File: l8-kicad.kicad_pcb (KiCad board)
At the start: 4 copper layers, 55.5 x 89.5 mm, 122 parts, among them J1 USB_B_Mini, J2 LCD 3.2" 240x320 Conn_01x14_P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, J3 Screw_Terminal_01x06, J4 Conn_ST_STDC14, J7 TC2030 - TAG Connect, Q1 SI2301CDS-T1-GE3, Q4 SI2301CDS-T1-GE3, Q5 SI2301CDS-T1-GE3, SW1 SW_Push, SW2 SW_Push, U1 B0505S-1WR2, U2 ISO1042-Q1, U22 TLV76733DRVx, U3 STM32F427V_G-I_Tx, U4 ST_SENSOR_2, U5 IIS3DHHCTR, X1 8MHz 20pF

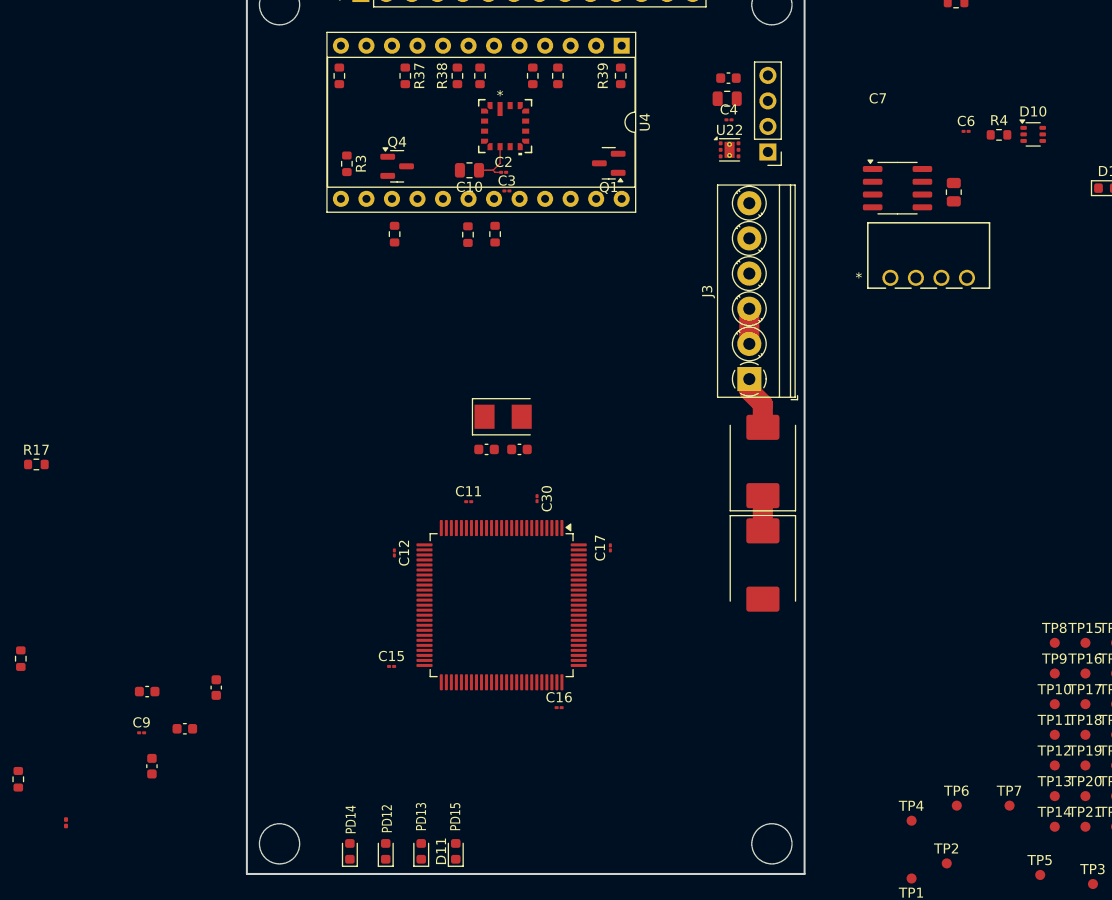
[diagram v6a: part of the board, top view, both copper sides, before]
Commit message: pre-quilter after cap size issue
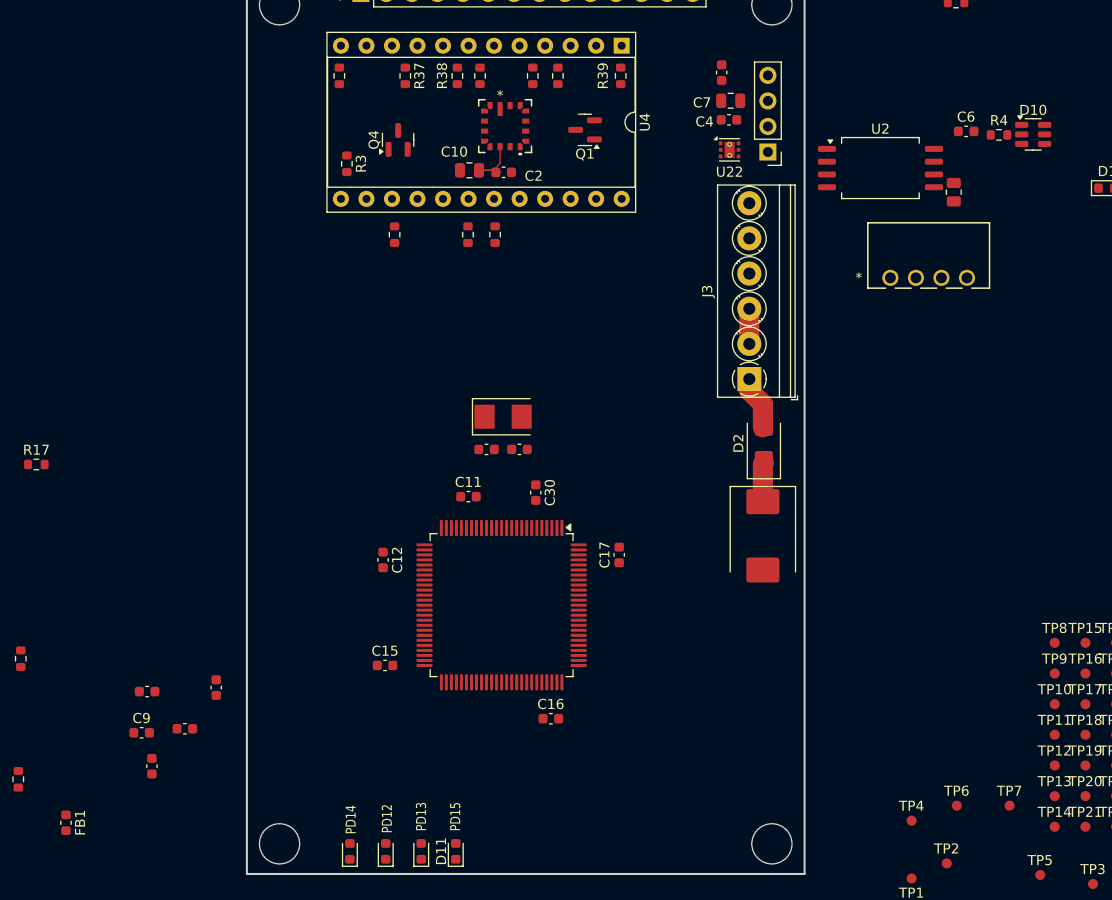
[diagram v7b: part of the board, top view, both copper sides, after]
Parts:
- removed C3: 100nF, Capacitor_SMD:C_01005_0402Metric
- C11, C12, C15, C16, C17, C2, C30, C4, C6, C9: footprint Capacitor_SMD:C_01005_0402Metric -> Capacitor_SMD:C_0603_1608Metric
- D10: footprint Package_TO_SOT_SMD:SOT-363_SC-70-6 -> Package_TO_SOT_SMD:SOT-23-6
- D2: footprint Diode_SMD:D_SMC -> Diode_SMD:D_SMA
- FB1: value FILTER -> ~; footprint Resistor_SMD:R_0201_0603Metric -> Inductor_SMD:L_0603_1608Metric
- U2: footprint Package_SO:SOIC-8_3.9x4.9mm_P1.27mm -> Package_SO:SOIC-8_7.5x5.85mm_P1.27mm
- moved Q1 4.08 mm to (133.7, 115.5)
- moved D3 2.90 mm to (151.3, 155.8)
- moved Q4 2.63 mm to (115.0, 116.5), turned to 90 degrees
- moved U2 2.62 mm to (163.1, 119.2)
- moved D2 1.80 mm to (151.4, 146.7)
- moved C16 1.38 mm to (130.2, 174.1)
- moved C12 1.32 mm to (113.5, 158.2)
- moved C17 1.12 mm to (137.1, 157.8)
- moved C5 0.87 mm to (147.2, 109.8), turned to -90 degrees
- moved C15 0.66 mm to (113.8, 168.8)
- moved C30 0.61 mm to (128.8, 151.6)
- moved C11 0.50 mm to (122.0, 151.9)
- moved C7 0.40 mm to (148.2, 112.5)

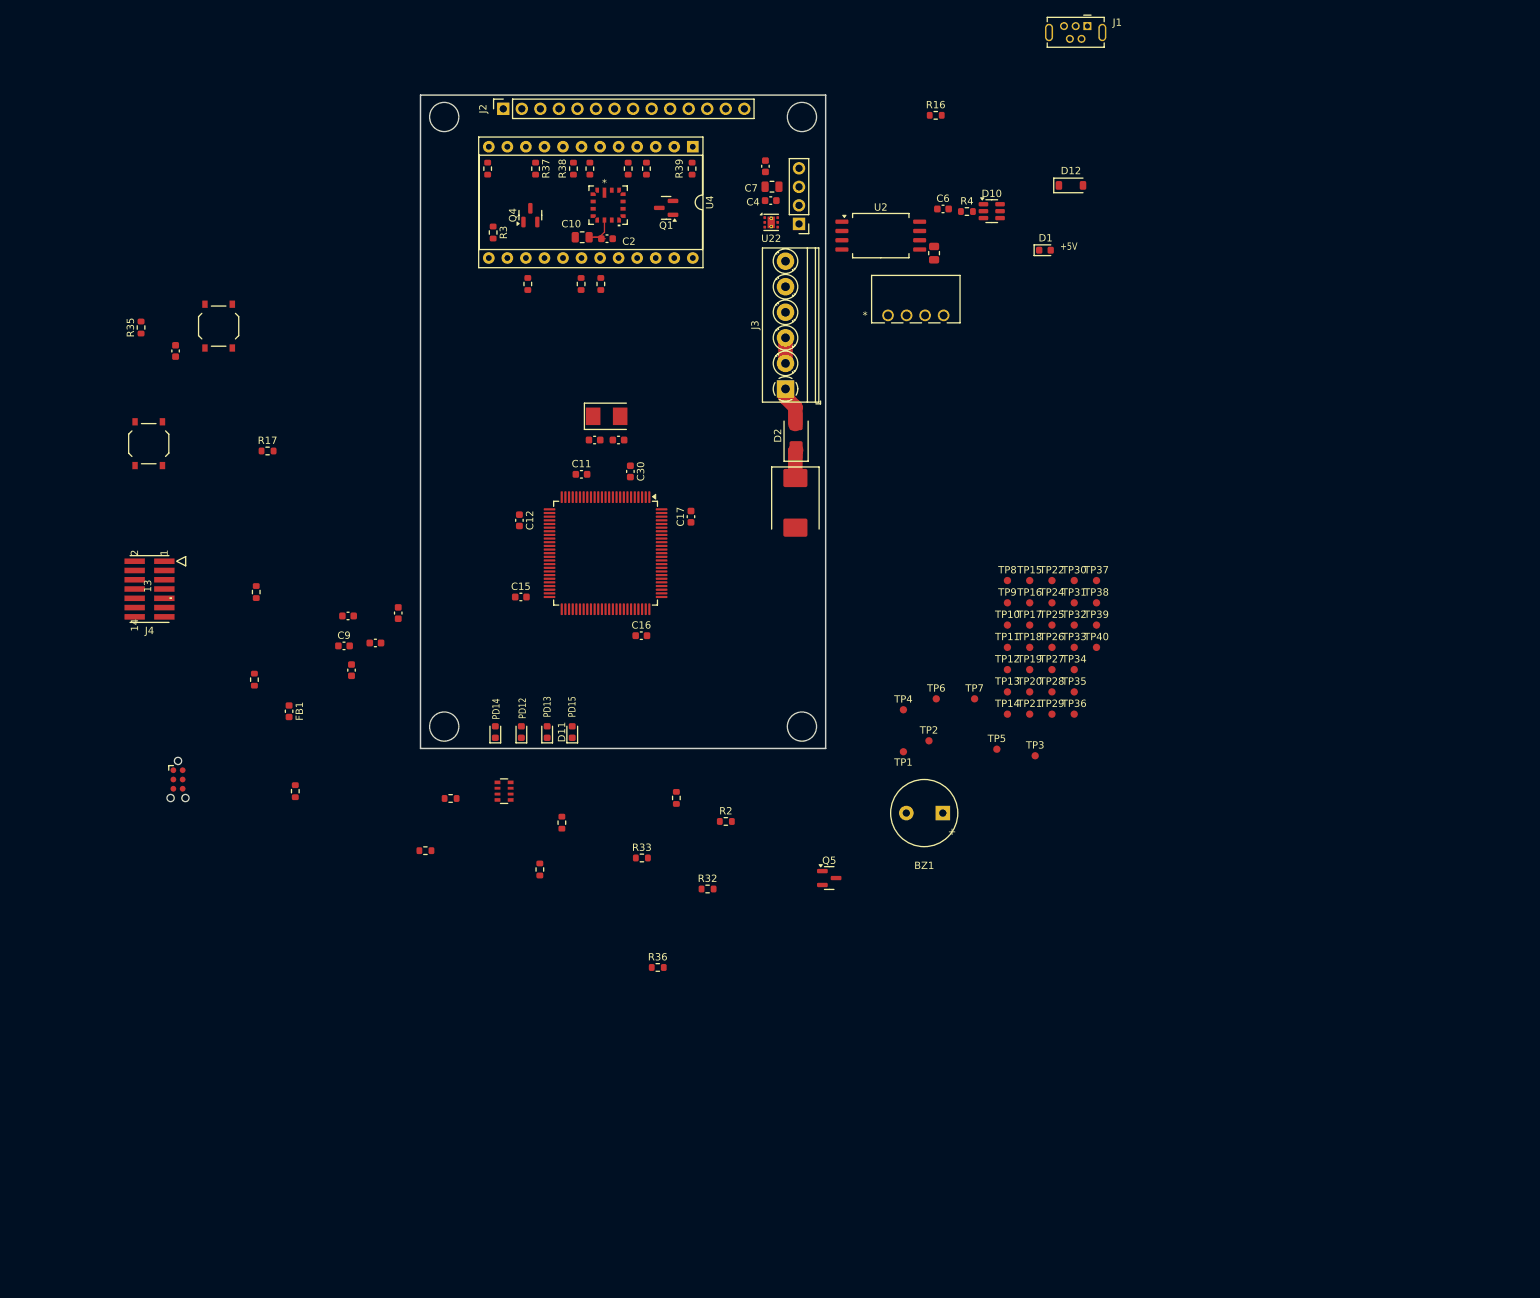
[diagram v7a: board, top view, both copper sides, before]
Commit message: remove tp and rotate cpu
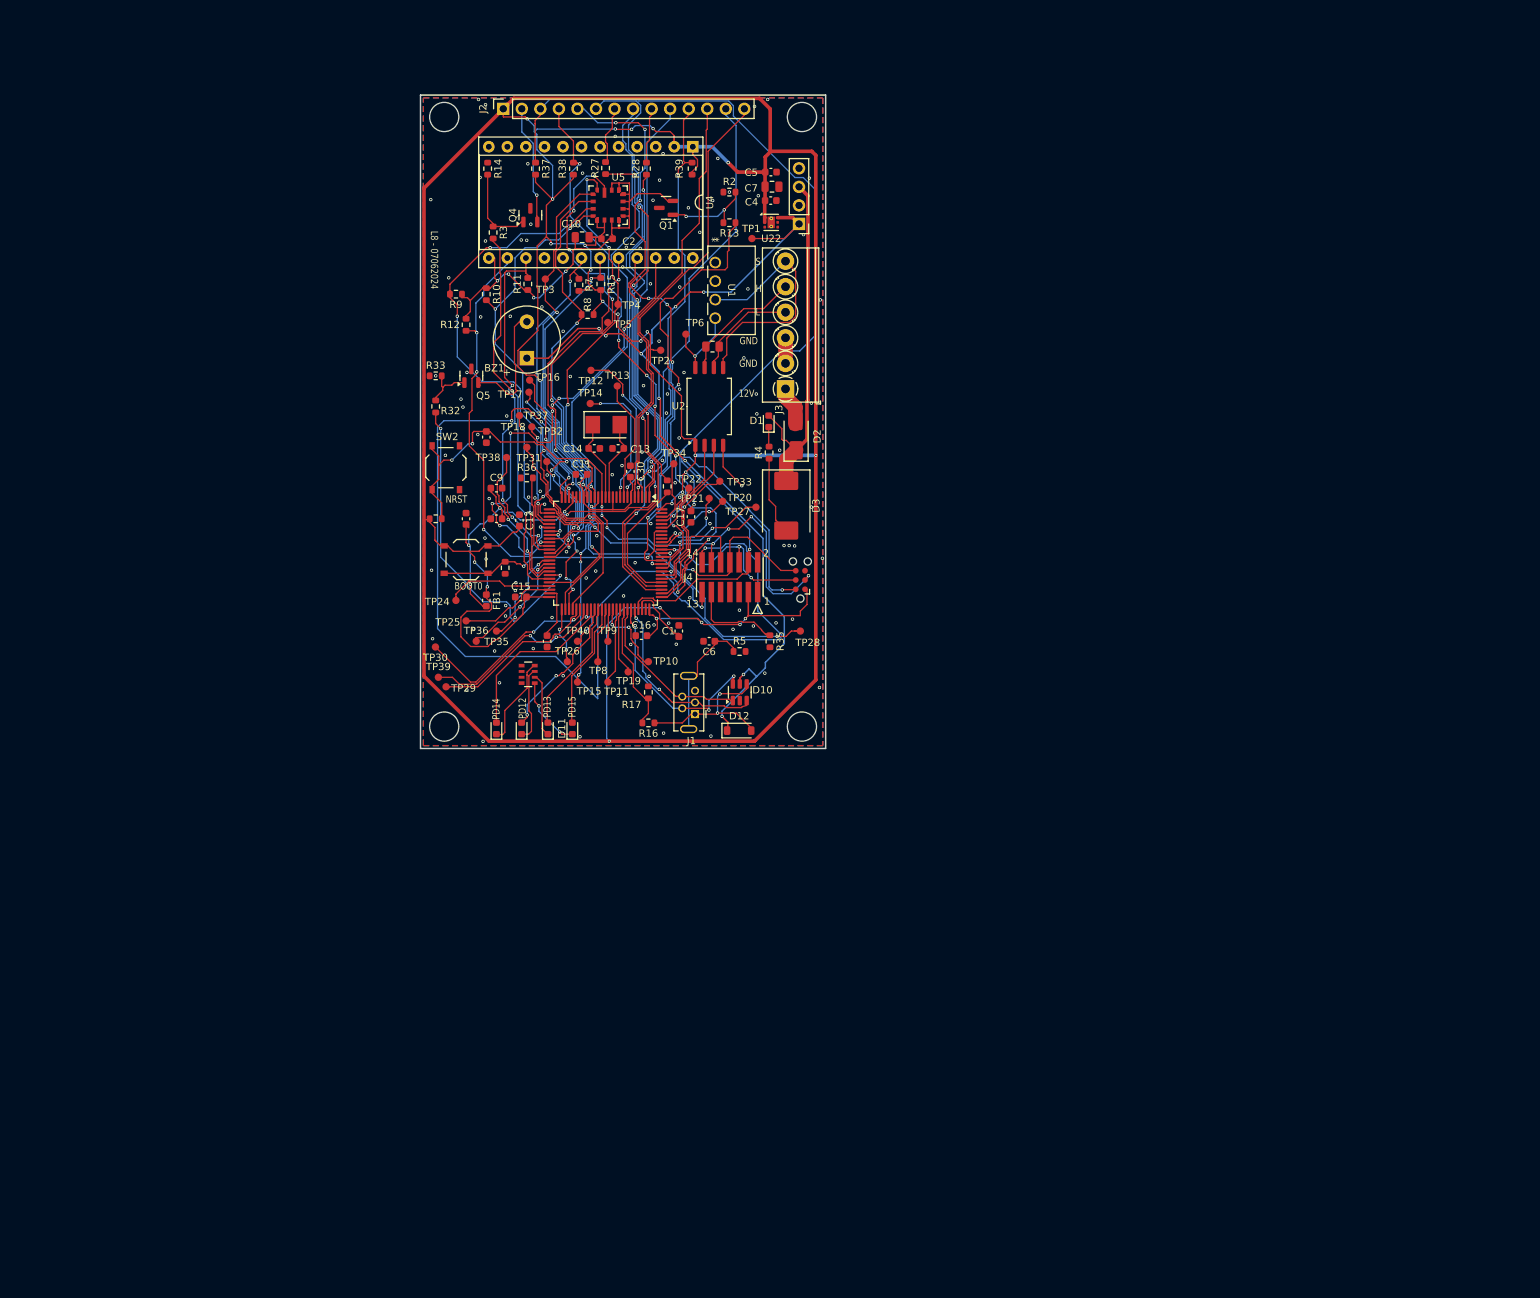
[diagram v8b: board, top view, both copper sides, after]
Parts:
- removed TP7: GND ISO, dnt:TestPoint_Pad_D1.0mm FP .6R
- moved J1 106.0 mm to (136.7, 183.2), turned to 90 degrees
- moved R35 96.3 mm to (147.9, 174.8), turned to -90 degrees
- moved TP3 93.6 mm to (117.1, 125.2), turned to 180 degrees
- moved R16 92.1 mm to (131.2, 186.0), turned to 180 degrees
- moved TP39 90.4 mm to (102.5, 179.8)
- moved J7 89.5 mm to (152.0, 166.4), turned to 90 degrees
- moved TP30 88.0 mm to (102.0, 175.6), turned to 180 degrees
- moved D12 87.4 mm to (143.7, 187.1)
- moved R2 86.2 mm to (142.3, 113.3)
- moved Q5 84.5 mm to (107.0, 138.4), turned to 90 degrees
- moved BZ1 84.4 mm to (114.6, 137.3), turned to 90 degrees
- moved TP38 83.2 mm to (111.8, 149.6), turned to 90 degrees
- moved TP29 83.1 mm to (103.5, 181.1), turned to 90 degrees
- moved TP36 82.5 mm to (107.6, 174.8)
- moved TP37 82.2 mm to (113.5, 143.9), turned to -90 degrees
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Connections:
- net Net-(U3-PC10) renamed /MCU/SPI3_SCK_*
- net Net-(U3-PC11) renamed /MCU/SPI3_SDI_*
- net Net-(U3-PC12) renamed /MCU/SPI3_SDO_*
- J3 pad 4: /CAN_H -> /CAN_L
- J3 pad 5: /CAN_L -> /CAN_H
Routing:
- net +3.3V: track 5.73 -> 642.5 mm, vias 0 -> 30
- net /MCU/USART2_TX: track 0.00 -> 149.3 mm, vias 0 -> 4
- net +5V: track 0.00 -> 127.7 mm, vias 0 -> 9
- net /SPI3_CS: track 0.00 -> 126.1 mm, vias 0 -> 3
- net /MCU/NRST: track 0.00 -> 88.9 mm, vias 0 -> 9
- net /LCD_LED: track 0.00 -> 80.6 mm, vias 0 -> 1
- net /SPI2_IRQ: track 0.00 -> 80.0 mm, vias 0 -> 6
- net /LCD_DC: track 0.00 -> 79.2 mm, vias 0 -> 7
- net /SPI2_SCK: track 0.00 -> 78.8 mm, vias 0 -> 6
- net /SPI2_IRQ2: track 0.00 -> 75.9 mm, vias 0 -> 3
- net /LCD_RESET: track 0.00 -> 75.4 mm, vias 0 -> 6
- net /SENSOR_ON: track 0.00 -> 71.6 mm, vias 0 -> 2
- net /MCU/SPI3_SCK_*: track 0.00 -> 70.8 mm, vias 0 -> 4
- net /SPI1_SDI: track 0.00 -> 65.5 mm, vias 0 -> 8
- net /MCU/SPI3_SDI_*: track 0.00 -> 65.4 mm, vias 0 -> 2
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- added copper zone on B.Cu, net GND
- added copper zone on F.Cu, net GND
- removed copper zone on In2.Cu, net +3.3V
- removed copper zone on In1.Cu, net GND
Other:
- copper layers 4 -> 2
- board text added: "1.85mm"
- board text added: "12V"
- board text added: "2"
- board text added: "BOOT0"
- board text added: "GND"
- board text added: "H"
- board text added: "L"
- board text added: "L8 - 07062024"
- board text added: "Manufacturer Recommendations"
- board text added: "NRST"
- board text added: "S"
- board text added: "STMicroelectronics"
- board text removed: "+5V"
